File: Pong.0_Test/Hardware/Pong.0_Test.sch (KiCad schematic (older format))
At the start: 25 parts, among them IC1 ATMEGA644P-A, J1 DC, J2 USB_2, P1 ISP, X1 20 MHz

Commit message: Updated Schematic and Project Log
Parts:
- removed J2: USB_2, symbol USB_2
- removed R2: 10k, symbol R
- added J2: USBMICRO-B, symbol USBMICRO-B
- added R10, R11, R12, R13, R14, R15, R16, R17, R18, R19, R20, R21, R22, R6, R7, R8, R9: 10K, symbol R
- added SW1: SPST, symbol SPST
- R3, R4, R5: value 10k -> 10K
- renumbered R6 to R2
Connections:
- net labels added: UU00, UU01, UU02, UU03, UU04, UU05, UU06, UU07, UU08, UU09, UU10, UU11, UU12, UU13, UU14, UU15, UU16, UU17, UU18, UU19
- wire segments 133 -> 158
- no-connect marks 2 -> 3

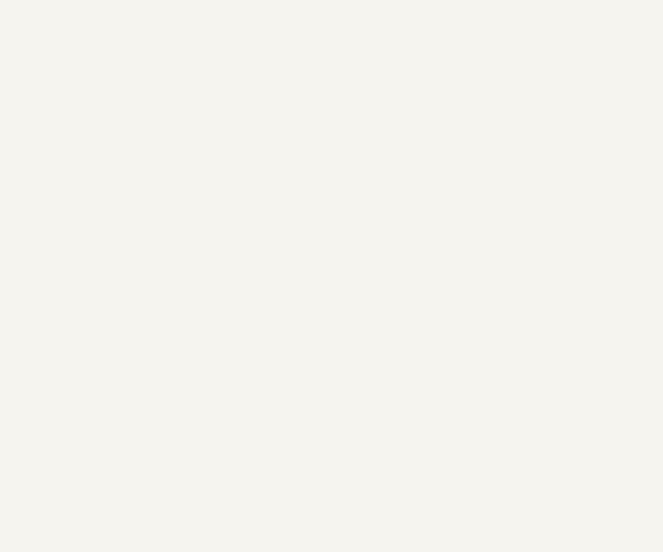
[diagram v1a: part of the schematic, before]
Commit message: Updated Project Log and added ATTiny84A for slider board testing
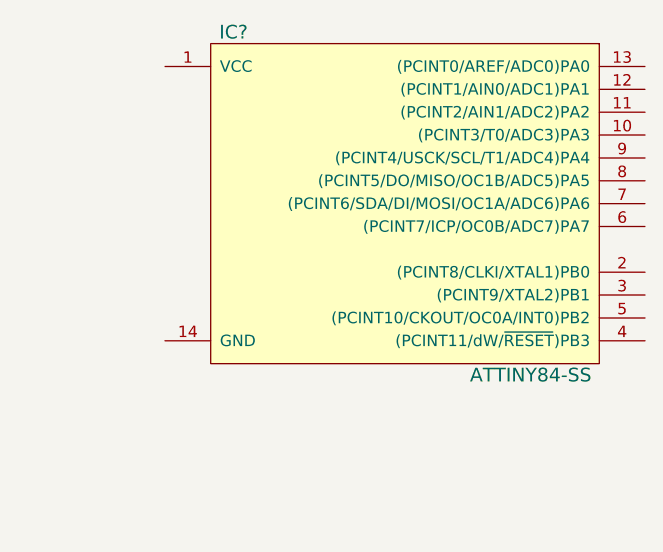
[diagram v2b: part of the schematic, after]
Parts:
- added IC?: ATTINY84-SS, SO14, symbol ATTINY84-SS
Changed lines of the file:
@@
-EESchema Schematic File Version 2  date 6/2/2012 2:18:36 PM
+EESchema Schematic File Version 2  date 7/3/2012 9:20:02 PM
 LIBS:power
 LIBS:device
@@
 Sheet 1 3
 Title "Pong.0 Test Board"
-Date "2 jun 2012"
+Date "4 jul 2012"
 Rev "1.0"
 Comp "Projects and Stuff LLC"
@@
 Comment4 ""
 $EndDescr
+$Comp
+L ATTINY84-SS IC?
+U 1 1 4FF39A32
+P 13200 1950
+F 0 "IC?" H 12450 2700 60  0000 C CNN
+F 1 "ATTINY84-SS" H 13750 1200 60  0000 C CNN
+F 2 "SO14" H 12500 1200 60  0001 C CNN
+	1    13200 1950
+	1    0    0    -1
+$EndComp
 Connection ~ 2100 1500
 Wire Wire Line
@@
 6E 56 52 49 51 4E 59 71 7E 65 C5 4D 0F AF 00 BF F6 21 9D BA 45 88 9C 00 16 00 C0 66 90 E0 00 00
 AC 42 3B 38 00 00 AB 90 E0 00 00 AC 42 82 03 00 B0 EA FF 00 E3 76 B5 A7 81 B6 BC 08 00 00 00 00
-49 45 4E 44 AE 42 60 82 8C $EndBitmap
+49 45 4E 44 AE 42 60 82 22 $EndBitmap
 EndData
 $EndBitmap

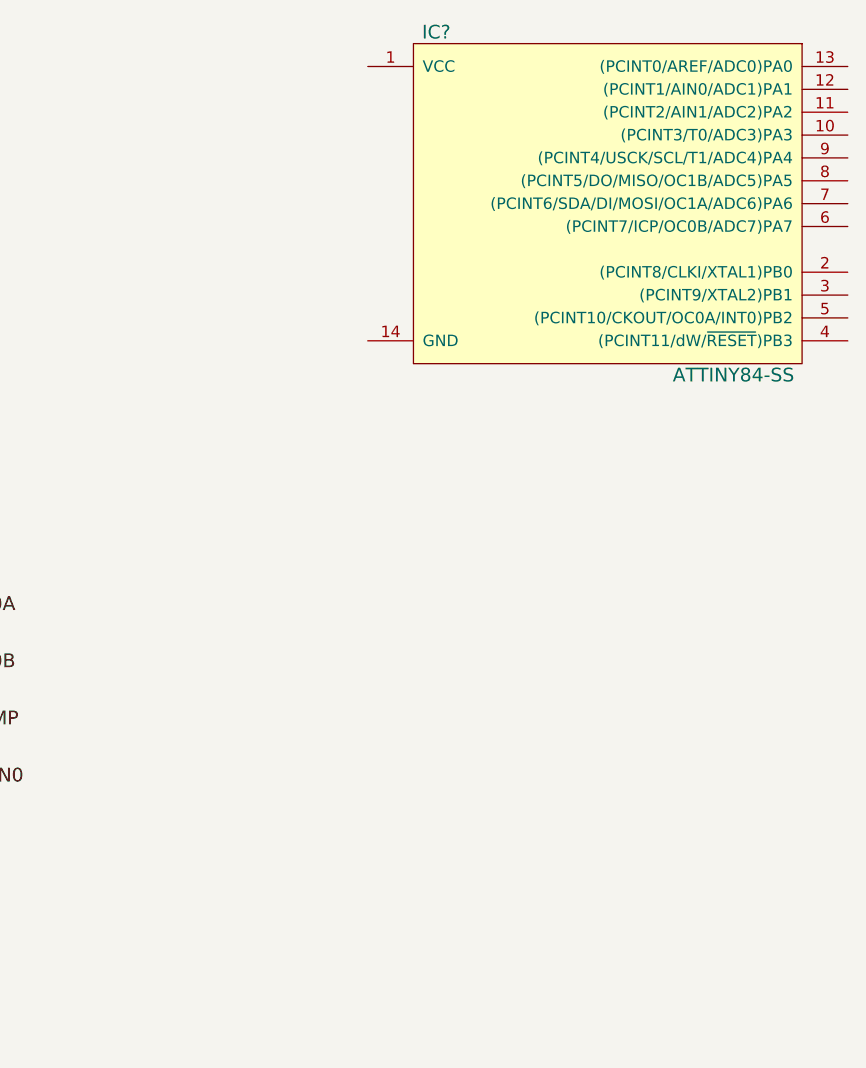
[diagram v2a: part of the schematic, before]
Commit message: Replaced ATTiny84 with ATMega168 for the added pins and peripherals
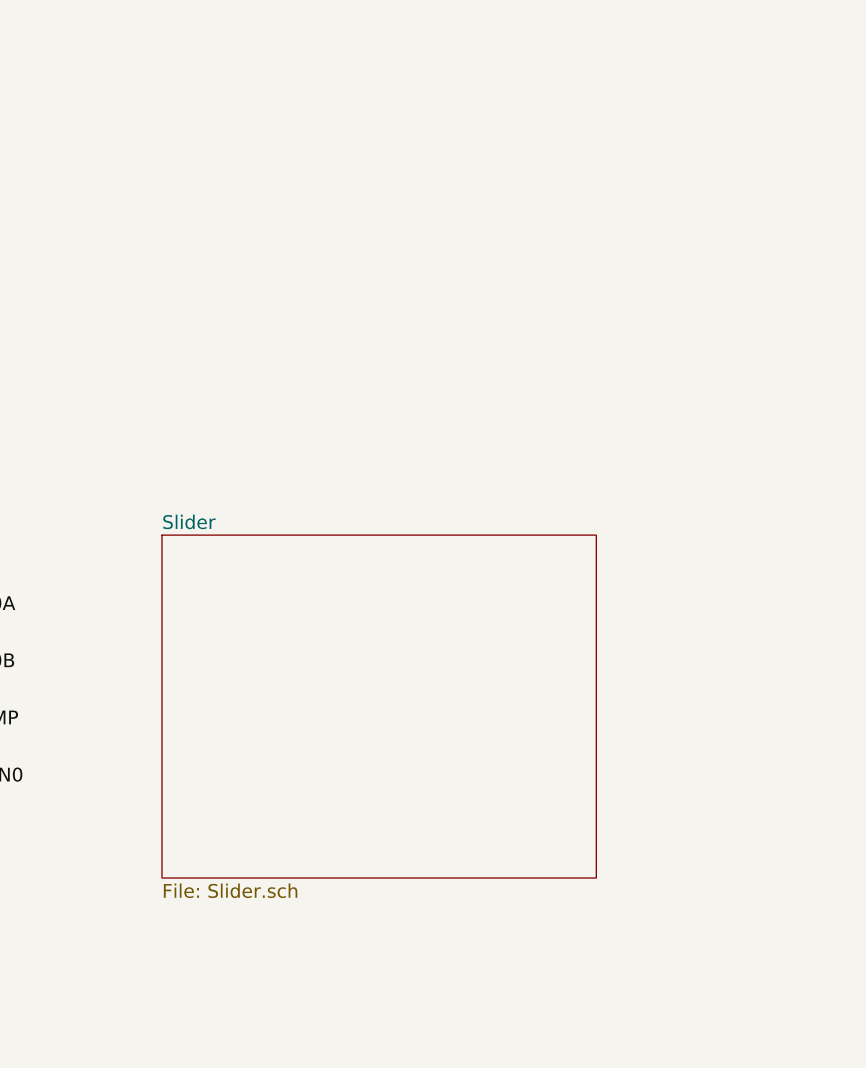
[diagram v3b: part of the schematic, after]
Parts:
- removed IC?: ATTINY84-SS, SO14, symbol ATTINY84-SS
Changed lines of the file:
@@
-EESchema Schematic File Version 2  date 7/3/2012 9:20:02 PM
+EESchema Schematic File Version 2  date 7/4/2012 1:10:30 PM
 LIBS:power
 LIBS:device
@@
 $Descr User 16000 11000
 encoding utf-8
-Sheet 1 3
+Sheet 1 4
 Title "Pong.0 Test Board"
 Date "4 jul 2012"
@@
 Comment4 ""
 $EndDescr
-$Comp
-L ATTINY84-SS IC?
-U 1 1 4FF39A32
-P 13200 1950
-F 0 "IC?" H 12450 2700 60  0000 C CNN
-F 1 "ATTINY84-SS" H 13750 1200 60  0000 C CNN
-F 2 "SO14" H 12500 1200 60  0001 C CNN
-	1    13200 1950
-	1    0    0    -1
-$EndComp
+$Sheet
+S 11250 3400 1900 1500
+U 4FF467AD
+F0 "Slider" 60
+F1 "Slider.sch" 60
+$EndSheet
 Connection ~ 2100 1500
 Wire Wire Line
@@
 6E 56 52 49 51 4E 59 71 7E 65 C5 4D 0F AF 00 BF F6 21 9D BA 45 88 9C 00 16 00 C0 66 90 E0 00 00
 AC 42 3B 38 00 00 AB 90 E0 00 00 AC 42 82 03 00 B0 EA FF 00 E3 76 B5 A7 81 B6 BC 08 00 00 00 00
-49 45 4E 44 AE 42 60 82 22 $EndBitmap
+49 45 4E 44 AE 42 60 82 15 $EndBitmap
 EndData
 $EndBitmap
